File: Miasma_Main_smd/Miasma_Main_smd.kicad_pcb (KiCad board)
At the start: 2 copper layers, 99.1 x 99.1 mm, 170 parts, among them P1 CONN_01X12, P2 CONN_01X10, P3 CONN_01X12, P4 CONN_01X10, P5 CONN_02X05, P6 CONN_01X01, P7 SUM_or_4QX, Q1 MMBT3904, Q2 MMBT3904, Q3 MMBT3904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

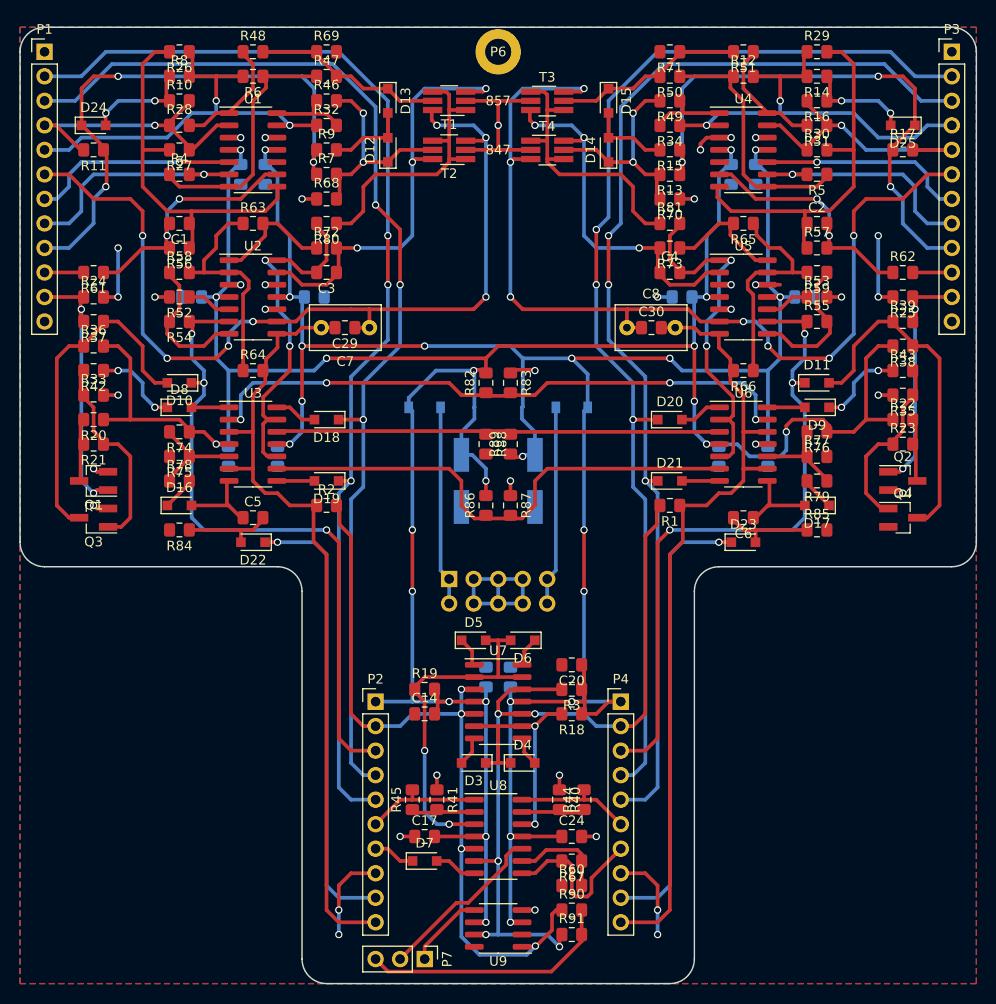
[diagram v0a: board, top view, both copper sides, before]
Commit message: Improve silkscreen of Miasma Main board
Silkscreen was unreadable on PCB because it was placed beneath components
or on top of other silkscreen. Rearrange silkscreen to make components
easier to place.

Kicad project has been saved as a Kicad 10 project now.

Exported iBOM.

Signed-off-by: Nicholas Marrone <nickmarrone@gmail.com>
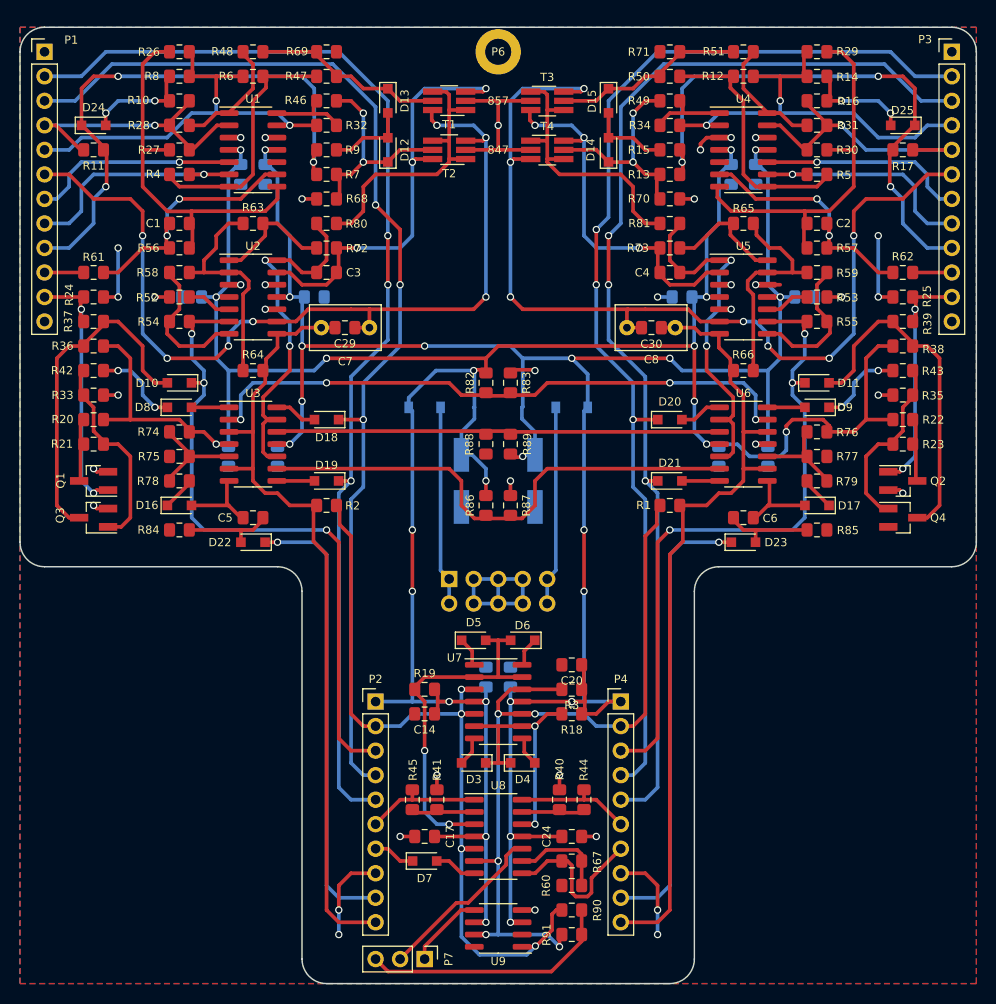
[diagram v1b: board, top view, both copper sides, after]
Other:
- net class Default removed
- board text added: "SIN PHI Miasma BEFACO Rampage CC BY-NC-SA 4.0 Version 1.04"
- board text removed: "SIN PHI Miasma BEFACO Rampage CC BY-NC-SA 4.0 Version 1.03"
